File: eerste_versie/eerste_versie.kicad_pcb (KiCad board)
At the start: 2 copper layers, 12 parts, among them U1 ESP32-WROOM-32U, U2 AMS1117-3.3, X1 DG3XX-02-5.0

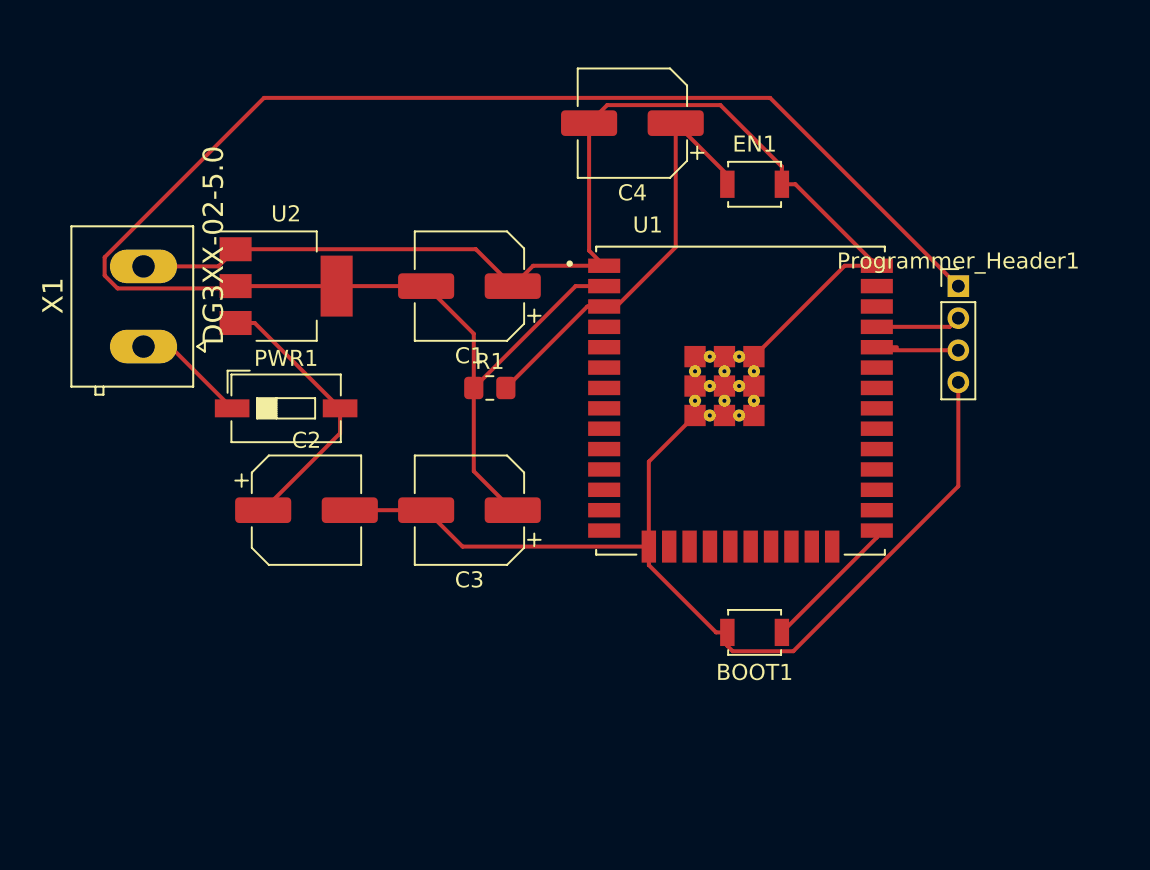
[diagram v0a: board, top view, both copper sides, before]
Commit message: 100n condensatoren van footprint gewijzigd
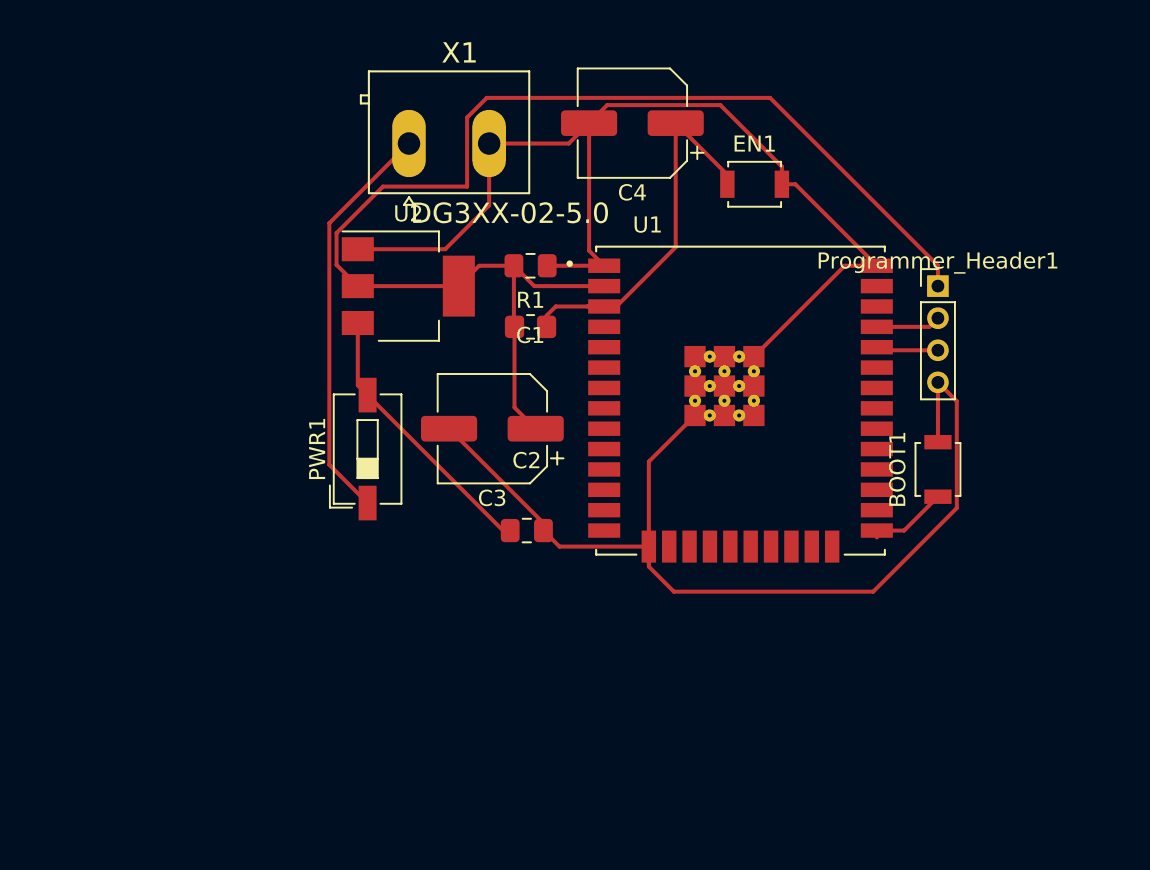
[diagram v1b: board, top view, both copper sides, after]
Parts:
- C1, C2: footprint Capacitor_SMD:CP_Elec_6.3x3 -> Capacitor_SMD:C_0805_2012Metric_Pad1.18x1.45mm_HandSolder
- moved X1 21.6 mm to (121.9, 99.1), turned to 0 degrees
- moved BOOT1 15.3 mm to (152.4, 119.4), turned to 90 degrees
- moved C2 13.8 mm to (126.8, 123.2)
- moved U2 7.62 mm to (119.4, 108.0)
- moved PWR1 5.68 mm to (116.8, 118.1), turned to 90 degrees
- moved C3 5.28 mm to (124.6, 116.8)
- moved R1 4.58 mm to (127.0, 110.5)
- moved C1 4.02 mm to (127.0, 106.7)
- moved Programmer_Header1 1.27 mm to (152.4, 108.0)
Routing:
- net VDD33: track 110.7 -> 80.1 mm
- net Net-(PWR1-Pad1): track 7.12 -> 25.5 mm
- net GND: track 158.9 -> 150.9 mm
- net Net-(C4-Pad1): track 27.1 -> 24.4 mm
- net Net-(Programmer_Header1-Pad3): track 6.41 -> 3.89 mm
- net Net-(BOOT1-Pad1): track 8.80 -> 6.64 mm
- net Net-(Programmer_Header1-Pad2): track 5.30 -> 4.03 mm

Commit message: tweede versie
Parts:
- added R2: 10k, Resistor_SMD:R_0805_2012Metric_Pad1.20x1.40mm_HandSolder, F.Cu at (152.4, 117.8)
- C4: value 47u -> 1u; footprint Capacitor_SMD:CP_Elec_6.3x3 -> Capacitor_SMD:C_0805_2012Metric_Pad1.18x1.45mm_HandSolder
- moved EN1 27.4 mm to (114.3, 108.0), turned to 270 degrees
- moved C4 22.2 mm to (128.3, 119.4), turned to 270 degrees
- moved X1 19.9 mm to (113.0, 116.8), turned to 90 degrees
- moved C2 11.5 mm to (118.1, 115.6), turned to 270 degrees
- moved PWR1 6.35 mm to (116.8, 124.5), turned to 0 degrees
- moved R1 4.02 mm to (128.3, 114.3), turned to 270 degrees
- moved BOOT1 3.81 mm to (152.4, 123.2)
- moved U2 2.84 mm to (121.9, 109.2)
- moved C3 1.91 mm to (123.2, 118.1), turned to 270 degrees
- moved C1 1.64 mm to (128.3, 107.7), turned to 270 degrees
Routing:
- net VDD33: track 80.1 -> 35.1 mm
- net Net-(PWR1-Pad1): track 25.5 -> 5.30 mm
- net Net-(C2-Pad1): track 17.1 -> 3.89 mm
- net Net-(C4-Pad1): track 24.4 -> 35.1 mm
- net Net-(BOOT1-Pad1): track 6.64 -> 12.3 mm
- net GND: track 150.9 -> 154.2 mm

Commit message: update
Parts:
- added BZ1: Buzzer, CPT-1255C-090:CUI_CPT-1255C-090, F.Cu at (148.6, 134.6)
- added D1: LED, LED_SMD:LED_0805_2012Metric_Pad1.15x1.40mm_HandSolder, F.Cu at (157.8, 129.4)
- added R3: TBD, Resistor_SMD:R_0805_2012Metric_Pad1.20x1.40mm_HandSolder, F.Cu at (157.7, 132.4)
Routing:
- net GND: track 154.2 -> 118.2 mm
- net VDD33: track 35.1 -> 57.6 mm
- net Net-(C4-Pad1): track 35.1 -> 12.7 mm

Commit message: derde_versie
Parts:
- added REF**: MountingHole_2.1mm, MountingHole:MountingHole_2.1mm, F.Cu at (157.5, 135.9)
- added REF**: MountingHole_2.1mm, MountingHole:MountingHole_2.1mm, F.Cu at (119.4, 106.7)
- added REF**: MountingHole_2.1mm, MountingHole:MountingHole_2.1mm, F.Cu at (157.5, 106.7)
- added REF**: MountingHole_2.1mm, MountingHole:MountingHole_2.1mm, F.Cu at (119.4, 135.9)
- moved X1 36.9 mm to (146.1, 133.3), turned to 180 degrees
- moved EN1 20.8 mm to (127.0, 124.5)
- moved R3 17.6 mm to (141.0, 127.0), turned to 180 degrees
- moved BZ1 15.4 mm to (133.4, 132.1)
- moved D1 13.2 mm to (144.8, 127.0), turned to 180 degrees
- moved PWR1 8.13 mm to (121.9, 130.8), turned to 180 degrees
- moved C2 6.84 mm to (124.5, 118.1), turned to 0 degrees
- moved Programmer_Header1 5.81 mm to (152.4, 113.8), turned to 180 degrees
- moved C3 5.68 mm to (120.7, 123.2)
- moved U2 3.81 mm to (121.9, 113.0)
- turned BOOT1 to 270 degrees
- turned C4 to 90 degrees
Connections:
- U1 pad 34: Net-(Programmer_Header1-Pad3) -> Net-(Programmer_Header1-Pad2)
- U1 pad 35: Net-(Programmer_Header1-Pad2) -> Net-(Programmer_Header1-Pad3)
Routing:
- net GND: track 118.2 -> 69.6 mm
- net Net-(PWR1-Pad1): track 5.30 -> 29.4 mm
- net Net-(C2-Pad1): track 3.89 -> 23.2 mm
- net Net-(BZ1-Pad1): track 0.00 -> 9.18 mm
- net Net-(R3-Pad2): track 0.00 -> 6.22 mm
- net Net-(C4-Pad1): track 12.7 -> 18.9 mm
- net Net-(BOOT1-Pad1): track 12.3 -> 7.93 mm
- net VDD33: track 57.6 -> 62.0 mm
- net Net-(D1-Pad2): track 0.00 -> 1.78 mm
- added copper zone on F.Cu, net GND
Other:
- board outline added: 43.2 x 34.3 mm

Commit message: volledige versie
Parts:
- removed X1: DG3XX-02-5.0, degson:degson-DG306-5.0-02P
- added C5: 100n, Capacitor_SMD:C_0805_2012Metric_Pad1.18x1.45mm_HandSolder, F.Cu at (125.7, 113.7)
- added J1: 105017-1001, 105017-1001:MOLEX_105017-1001, F.Cu at (135.1, 135.9)
- BOOT1, EN1: footprint Button_Switch_SMD:SW_SPST_B3U-1000P -> 434111043826:434111043826
- C2: value 100n -> 10uF
- C3: value 47u -> 10uF; footprint Capacitor_SMD:CP_Elec_6.3x3 -> Capacitor_SMD:C_0805_2012Metric_Pad1.18x1.45mm_HandSolder
- PWR1: footprint Button_Switch_SMD:SW_DIP_SPSTx01_Slide_6.7x4.1mm_W6.73mm_P2.54mm_LowProfile_JPin -> sparkfun:SWITCH_SPST_SMD_A
- Prog_head1: renamed from Programmer_Header1; footprint Connector_PinHeader_2.00mm:PinHeader_1x04_P2.00mm_Vertical -> Connector_PinHeader_2.54mm:PinHeader_1x04_P2.54mm_Vertical
- moved BZ1 12.7 mm to (146.1, 132.1)
- moved C2 12.2 mm to (132.1, 127.6)
- moved C3 9.83 mm to (123.1, 113.7), turned to 90 degrees
- moved U2 9.07 mm to (125.7, 121.3), turned to 90 degrees
- moved C4 8.91 mm to (127.6, 110.5), turned to 180 degrees
- moved D1 8.49 mm to (136.9, 130.2), turned to 0 degrees
- moved PWR1 7.47 mm to (126.2, 136.9)
- moved EN1 6.63 mm to (125.1, 130.8), turned to 0 degrees
- moved BOOT1 4.16 mm to (154.6, 126.7)
- moved R3 4.11 mm to (136.9, 127.6)
- moved R2 1.92 mm to (151.8, 119.7)
- moved Prog_head1 1.27 mm to (152.4, 115.0)
- moved UR 0.90 mm to (156.8, 107.3)
- moved R1 0.74 mm to (128.7, 113.7), turned to 90 degrees
- moved C1 0.72 mm to (128.5, 107.0)
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- renumbered REF** to DL, REF** to DR, REF** to UL, REF** to UR
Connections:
- U1 pad 14: Net-(BZ1-Pad1) -> Net-(U1-Pad14)
- U1 pad 23: Net-(U1-Pad23) -> Net-(BZ1-Pad1)
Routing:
- net Net-(J1-Pad1): track 29.4 -> 9.00 mm
- net Net-(C4-Pad1): track 18.9 -> 34.3 mm, vias 0 -> 2
- net GND: track 69.6 -> 77.6 mm
- net Net-(C2-Pad1): track 23.2 -> 16.0 mm
- net Net-(R3-Pad2): track 6.22 -> 3.55 mm
- net Net-(BOOT1-Pad1): track 7.93 -> 9.62 mm
- net VDD33: track 62.0 -> 60.8 mm, vias 0 -> 3
- net Net-(BZ1-Pad1): track 9.18 -> 8.30 mm
- net Net-(D1-Pad2): track 1.78 -> 2.55 mm
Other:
- board size 43.2 x 34.3 mm -> 42.5 x 33.7 mm
- net class Default: trace_width 0.25 -> 0.254
- rule trace_min: 0.2 -> 0.1524

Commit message: om te printen
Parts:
- Prog_head1: footprint Connector_PinHeader_2.54mm:PinHeader_1x04_P2.54mm_Vertical -> Connector_PinSocket_2.54mm:PinSocket_1x04_P2.54mm_Vertical
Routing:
- removed copper zone on F.Cu, net GND
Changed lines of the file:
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@@
   )
   (setup
-    (last_trace_width 0.635)
+    (last_trace_width 0.254)
     (user_trace_width 0.254)
     (user_trace_width 0.635)
@@
     (add_net VDD33)
   )
+  (module Connector_PinSocket_2.54mm:PinSocket_1x04_P2.54mm_Vertical (layer F.Cu)
+    (at 152.4 115.03 180)
+    (descr "Through hole straight socket strip, 1x04, 2.54mm pitch, single row (from Kicad 4.0.7), script generated")
+    (tags "Through hole socket strip THT 1x04 2.54mm single row")
+    (fp_text reference Prog_head1 (at 0 -2.77) (layer F.SilkS)
+      (effects (font (size 1 1) (thickness 0.15)))
+    )
+    (fp_text value Conn_01x04 (at 0 10.39) (layer F.Fab)
+      (effects (font (size 1 1) (thickness 0.15)))
+    )
+    (fp_text user %R (at 0 3.81 90) (layer F.Fab)
+      (effects (font (size 1 1) (thickness 0.15)))
+    )
+    (fp_line (start -1.27 -1.27) (end 0.635 -1.27) (layer F.Fab) (width 0.1))
+    (fp_line (start 0.635 -1.27) (end 1.27 -0.635) (layer F.Fab) (width 0.1))
+    (fp_line (start 1.27 -0.635) (end 1.27 8.89) (layer F.Fab) (width 0.1))
+    (fp_line (start 1.27 8.89) (end -1.27 8.89) (layer F.Fab) (width 0.1))
+    (fp_line (start -1.27 8.89) (end -1.27 -1.27) (layer F.Fab) (width 0.1))
+    (fp_line (start -1.33 1.27) (end 1.33 1.27) (layer F.SilkS) (width 0.12))
+    (fp_line (start -1.33 1.27) (end -1.33 8.95) (layer F.SilkS) (width 0.12))
+    (fp_line (start -1.33 8.95) (end 1.33 8.95) (layer F.SilkS) (width 0.12))
+    (fp_line (start 1.33 1.27) (end 1.33 8.95) (layer F.SilkS) (width 0.12))
+    (fp_line (start 1.33 -1.33) (end 1.33 0) (layer F.SilkS) (width 0.12))
+    (fp_line (start 0 -1.33) (end 1.33 -1.33) (layer F.SilkS) (width 0.12))
+    (fp_line (start -1.8 -1.8) (end 1.75 -1.8) (layer F.CrtYd) (width 0.05))
+    (fp_line (start 1.75 -1.8) (end 1.75 9.4) (layer F.CrtYd) (width 0.05))
+    (fp_line (start 1.75 9.4) (end -1.8 9.4) (layer F.CrtYd) (width 0.05))
+    (fp_line (start -1.8 9.4) (end -1.8 -1.8) (layer F.CrtYd) (width 0.05))
+    (pad 4 thru_hole oval (at 0 7.62 180) (size 1.7 1.7) (drill 1) (layers *.Cu *.Mask)
+      (net 1 GND))
+    (pad 3 thru_hole oval (at 0 5.08 180) (size 1.7 1.7) (drill 1) (layers *.Cu *.Mask)
+      (net 40 "Net-(Prog_head1-Pad3)"))
+    (pad 2 thru_hole oval (at 0 2.54 180) (size 1.7 1.7) (drill 1) (layers *.Cu *.Mask)
+      (net 41 "Net-(Prog_head1-Pad2)"))
+    (pad 1 thru_hole rect (at 0 0 180) (size 1.7 1.7) (drill 1) (layers *.Cu *.Mask)
+      (net 3 VDD33))
+    (model ${KISYS3DMOD}/Connector_PinSocket_2.54mm.3dshapes/PinSocket_1x04_P2.54mm_Vertical.wrl
+      (at (xyz 0 0 0))
+      (scale (xyz 1 1 1))
+      (rotate (xyz 0 0 0))
+    )
+  )
   (module Capacitor_SMD:C_0805_2012Metric_Pad1.18x1.45mm_HandSolder (layer F.Cu)
     (at 125.73 113.665 270)
@@
       (net 3 VDD33))
     (model ${KISYS3DMOD}/Capacitor_SMD.3dshapes/C_0805_2012Metric.wrl
-      (at (xyz 0 0 0))
-      (scale (xyz 1 1 1))
-      (rotate (xyz 0 0 0))
-    )
-  )
-  (module Connector_PinHeader_2.54mm:PinHeader_1x04_P2.54mm_Vertical (layer F.Cu)
-    (at 152.4 115.03 180)
-    (descr "Through hole straight pin header, 1x04, 2.54mm pitch, single row")
-    (tags "Through hole pin header THT 1x04 2.54mm single row")
-    (fp_text reference Prog_head1 (at -2.54 1.365 90) (layer F.SilkS)
-      (effects (font (size 1 1) (thickness 0.15)))
-    )
-    (fp_text value Conn_01x04 (at 0 9.95) (layer F.Fab)
-      (effects (font (size 1 1) (thickness 0.15)))
-    )
-    (fp_line (start 1.8 -1.8) (end -1.8 -1.8) (layer F.CrtYd) (width 0.05))
-    (fp_line (start 1.8 9.4) (end 1.8 -1.8) (layer F.CrtYd) (width 0.05))
-    (fp_line (start -1.8 9.4) (end 1.8 9.4) (layer F.CrtYd) (width 0.05))
-    (fp_line (start -1.8 -1.8) (end -1.8 9.4) (layer F.CrtYd) (width 0.05))
-    (fp_line (start -1.33 -1.33) (end 0 -1.33) (layer F.SilkS) (width 0.12))
-    (fp_line (start -1.33 0) (end -1.33 -1.33) (layer F.SilkS) (width 0.12))
-    (fp_line (start -1.33 1.27) (end 1.33 1.27) (layer F.SilkS) (width 0.12))
-    (fp_line (start 1.33 1.27) (end 1.33 8.95) (layer F.SilkS) (width 0.12))
-    (fp_line (start -1.33 1.27) (end -1.33 8.95) (layer F.SilkS) (width 0.12))
-    (fp_line (start -1.33 8.95) (end 1.33 8.95) (layer F.SilkS) (width 0.12))
-    (fp_line (start -1.27 -0.635) (end -0.635 -1.27) (layer F.Fab) (width 0.1))
-    (fp_line (start -1.27 8.89) (end -1.27 -0.635) (layer F.Fab) (width 0.1))
-    (fp_line (start 1.27 8.89) (end -1.27 8.89) (layer F.Fab) (width 0.1))
-    (fp_line (start 1.27 -1.27) (end 1.27 8.89) (layer F.Fab) (width 0.1))
-    (fp_line (start -0.635 -1.27) (end 1.27 -1.27) (layer F.Fab) (width 0.1))
-    (fp_text user %R (at 0 3.81 90) (layer F.Fab)
-      (effects (font (size 1 1) (thickness 0.15)))
-    )
-    (pad 4 thru_hole oval (at 0 7.62 180) (size 1.7 1.7) (drill 1) (layers *.Cu *.Mask)
-      (net 1 GND))
-    (pad 3 thru_hole oval (at 0 5.08 180) (size 1.7 1.7) (drill 1) (layers *.Cu *.Mask)
-      (net 40 "Net-(Prog_head1-Pad3)"))
-    (pad 2 thru_hole oval (at 0 2.54 180) (size 1.7 1.7) (drill 1) (layers *.Cu *.Mask)
-      (net 41 "Net-(Prog_head1-Pad2)"))
-    (pad 1 thru_hole rect (at 0 0 180) (size 1.7 1.7) (drill 1) (layers *.Cu *.Mask)
-      (net 3 VDD33))
-    (model ${KISYS3DMOD}/Connector_PinHeader_2.54mm.3dshapes/PinHeader_1x04_P2.54mm_Vertical.wrl
       (at (xyz 0 0 0))
       (scale (xyz 1 1 1))
@@
       (effects (font (size 1 1) (thickness 0.15)))
     )
-    (fp_text user %R (at 0.3 0) (layer F.Fab)
-      (effects (font (size 1 1) (thickness 0.15)))
-    )
     (fp_circle (center 0 0) (end 2.1 0) (layer Cmts.User) (width 0.15))
     (fp_circle (center 0 0) (end 2.35 0) (layer F.CrtYd) (width 0.05))
+    (fp_text user %R (at 0.3 0) (layer F.Fab)
+      (effects (font (size 1 1) (thickness 0.15)))
+    )
     (pad "" np_thru_hole circle (at 0 0) (size 2.1 2.1) (drill 2.1) (layers *.Cu *.Mask))
   )
@@
   (segment (start 121.745 126.54) (end 133.985 114.3) (width 0.635) (layer B.Cu) (net 5))
   (segment (start 121.745 127.81) (end 121.745 126.54) (width 0.635) (layer B.Cu) (net 5))
-  (segment (start 151.86 110.49) (end 148.59 110.49) (width 0.635) (layer F.Cu) (net 40))
-  (segment (start 152.4 109.95) (end 151.86 110.49) (width 0.635) (layer F.Cu) (net 40))
-  (segment (start 151.67 111.76) (end 148.59 111.76) (width 0.635) (layer F.Cu) (net 41))
-  (segment (start 152.4 112.49) (end 151.67 111.76) (width 0.635) (layer F.Cu) (net 41))
   (segment (start 144.535 131.095) (end 143.55 132.08) (width 0.635) (layer F.Cu) (net 32))
   (segment (start 144.535 124.19) (end 144.535 131.095) (width 0.635) (layer F.Cu) (net 32))
@@
   (segment (start 133.671 131.445) (end 133.828 131.602) (width 0.4) (layer F.Cu) (net 38))
   (segment (start 131.445 131.445) (end 133.671 131.445) (width 0.4) (layer F.Cu) (net 38))
-  (zone (net 1) (net_name GND) (layer F.Cu) (hatch edge 0.508)
-    (connect_pads (clearance 0.508))
-    (min_thickness 0.254)
-    (fill yes (arc_segments 32) (thermal_gap 0.508) (thermal_bridge_width 0.508))
-    (polygon
-      (pts
-        (xy 159.385 138.43) (xy 116.84 138.43) (xy 116.84 104.775) (xy 159.385 104.775)
-      )
-    )
-  )
+  (segment (start 151.86 110.49) (end 148.59 110.49) (width 0.635) (layer F.Cu) (net 40))
+  (segment (start 152.4 109.95) (end 151.86 110.49) (width 0.635) (layer F.Cu) (net 40))
+  (segment (start 151.67 111.76) (end 148.59 111.76) (width 0.635) (layer F.Cu) (net 41))
+  (segment (start 152.4 112.49) (end 151.67 111.76) (width 0.635) (layer F.Cu) (net 41))
 )

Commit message: om te printen 2
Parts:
- moved C4 2.54 mm to (125.1, 110.5)
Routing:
- net Net-(C4-Pad1): track 34.3 -> 26.8 mm
- net VDD33: track 60.8 -> 65.5 mm, vias 3 -> 2
